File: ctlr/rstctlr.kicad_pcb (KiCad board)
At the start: 2 copper layers, 114.3 x 63.5 mm, 95 parts, among them J1 USB_B, J3 ICSP, U1 FT232RL, U10 LTV-827S, U11 LTV-827S, U12 LTV-827S, U2 MIC2025-1YM, U3 ATtiny2313A-20SU, U4 TLC59281, U5 LTV-827S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

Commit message: Update to KiCad6.
Signed-off-by: Dan Cross <cross@gajendra.net>
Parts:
- moved C4 7.93 mm to (78.2, 72.7)
- moved C5 7.93 mm to (86.8, 83.7)
- moved J3 7.93 mm to (97.0, 88.8)
- moved R7 7.93 mm to (93.5, 72.7)
- moved R8 7.93 mm to (101.7, 77.6)
- moved U1 7.93 mm to (80.3, 80.4)
- moved C2 7.93 mm to (75.8, 71.9)
- moved C3 7.93 mm to (80.5, 71.9)
- moved FB1 7.93 mm to (78.2, 71.9)
- moved R6 7.93 mm to (83.9, 71.9)
- moved C6 7.93 mm to (93.5, 77.0)
- moved C7 7.93 mm to (98.6, 69.9)
- moved D4 7.93 mm to (79.8, 88.6)
- moved D5 7.93 mm to (84.3, 88.6)
- moved J2 7.93 mm to (87.5, 67.9)
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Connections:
- U1 pad 10: Net-(U1-Pad10) -> unconnected-(U1-Pad10)
- U1 pad 11: Net-(U1-Pad11) -> unconnected-(U1-Pad11)
- U1 pad 13: Net-(U1-Pad13) -> unconnected-(U1-Pad13)
- U1 pad 2: Net-(U1-Pad2) -> unconnected-(U1-Pad2)
- U1 pad 24: Net-(U1-Pad24) -> unconnected-(U1-Pad24)
- U1 pad 27: Net-(U1-Pad27) -> unconnected-(U1-Pad27)
- U1 pad 28: Net-(U1-Pad28) -> unconnected-(U1-Pad28)
- U1 pad 3: Net-(U1-Pad3) -> unconnected-(U1-Pad3)
- U1 pad 6: Net-(U1-Pad6) -> unconnected-(U1-Pad6)
- U1 pad 8: Net-(U1-Pad8) -> unconnected-(U1-Pad8)
- U1 pad 9: Net-(U1-Pad9) -> unconnected-(U1-Pad9)
- U2 pad 2: Net-(U2-Pad2) -> unconnected-(U2-Pad2)
- U2 pad 4: Net-(U2-Pad4) -> unconnected-(U2-Pad4)
- U2 pad 5: Net-(U2-Pad5) -> unconnected-(U2-Pad5)
- U3 pad 11: Net-(U3-Pad11) -> unconnected-(U3-Pad11)
- U3 pad 16: Net-(U3-Pad16) -> unconnected-(U3-Pad16)
- U3 pad 4: Net-(U3-Pad4) -> unconnected-(U3-Pad4)
- U3 pad 6: Net-(U3-Pad6) -> unconnected-(U3-Pad6)
- U3 pad 7: Net-(U3-Pad7) -> unconnected-(U3-Pad7)
- U3 pad 8: Net-(U3-Pad8) -> unconnected-(U3-Pad8)
- U3 pad 9: Net-(U3-Pad9) -> unconnected-(U3-Pad9)
- U4 pad 22: Net-(U4-Pad22) -> unconnected-(U4-Pad22)
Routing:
- net Net-(C6-Pad1): track 289.3 -> 278.1 mm
- net Net-(D3-Pad1): track 13.8 -> 6.69 mm
- net Net-(C2-Pad1): track 15.0 -> 8.52 mm
- net Net-(D2-Pad1): track 16.1 -> 9.70 mm
- net Net-(U3-Pad13): track 38.8 -> 40.6 mm
- net Net-(J3-Pad5): track 25.6 -> 26.7 mm
- net Net-(R8-Pad1): track 37.3 -> 38.4 mm
- net Net-(U3-Pad12): track 35.1 -> 36.1 mm
- net Net-(D41-Pad1): track 10.8 -> 9.90 mm
- net Net-(D21-Pad2): track 5.61 -> 4.75 mm
- net Net-(D40-Pad1): track 9.78 -> 8.92 mm
- net Net-(D43-Pad1): track 10.9 -> 10.1 mm
- net Net-(D39-Pad1): track 10.9 -> 10.1 mm
- net Net-(D19-Pad1): track 13.0 -> 12.2 mm
- net Net-(D40-Pad2): track 9.71 -> 8.96 mm
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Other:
- net class Default removed

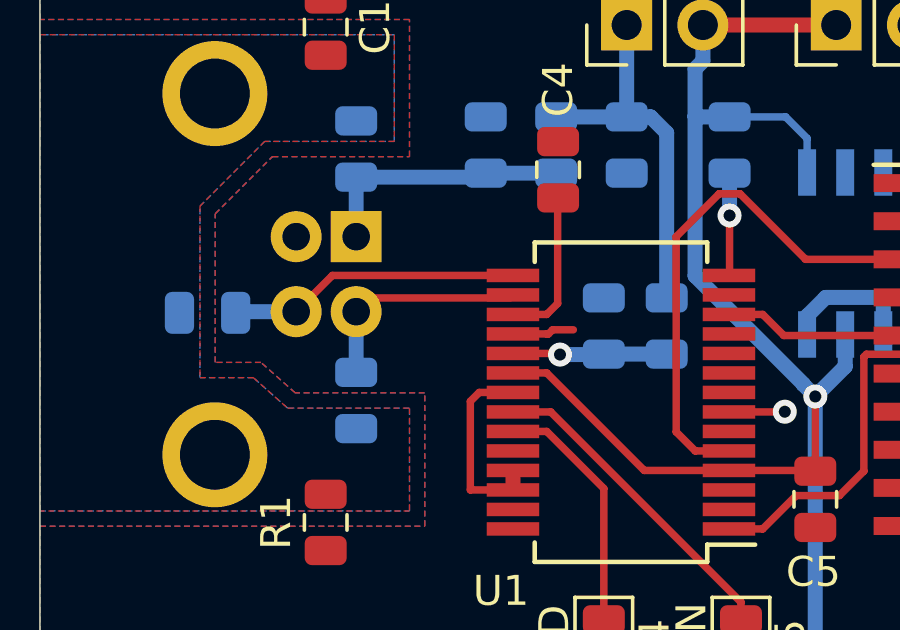
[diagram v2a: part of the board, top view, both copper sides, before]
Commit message: rstctlr: adjust USB trace length, fix stylesheets
Signed-off-by: Dan Cross <cross@gajendra.net>
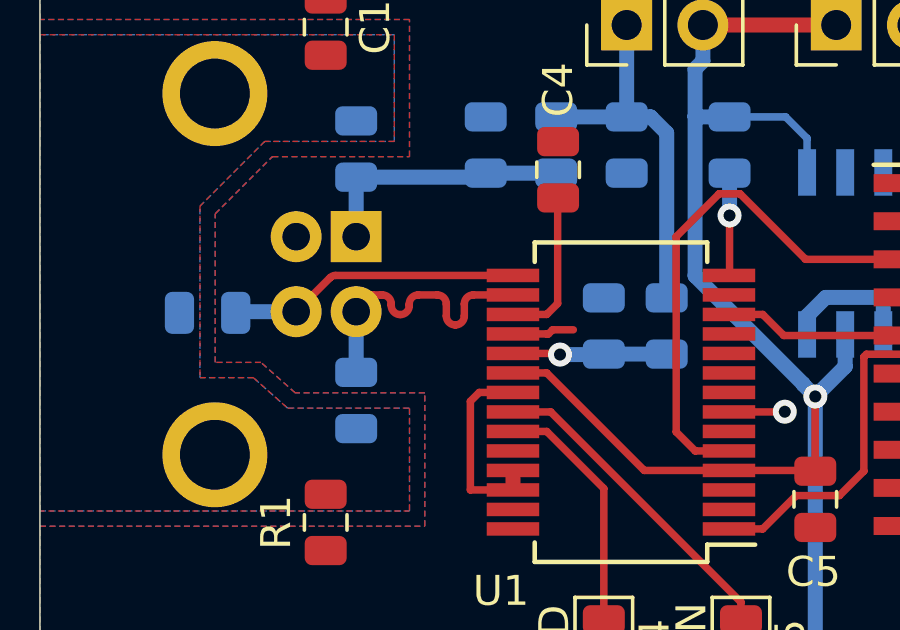
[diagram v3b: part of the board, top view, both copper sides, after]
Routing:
- net Net-(D3-Pad1): track 6.69 -> 9.66 mm
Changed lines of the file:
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@@
   (segment (start 92.5345 76.955) (end 89.027 76.955) (width 0.5) (layer "B.Cu") (net 6))
   (segment (start 86.53142 77.575137) (end 86.53142 78.665139) (width 0.5) (layer "B.Cu") (net 6))
-  (segment (start 70.7085 76.2225) (end 76.7275 76.2225) (width 0.25) (layer "F.Cu") (net 7))
-  (segment (start 69.501 77.43) (end 70.7085 76.2225) (width 0.25) (layer "F.Cu") (net 7))
+  (segment (start 70.635276 76.295724) (end 69.501 77.43) (width 0.25) (layer "F.Cu") (net 7))
+  (segment (start 76.7275 76.2225) (end 70.812053 76.2225) (width 0.25) (layer "F.Cu") (net 7))
+  (arc (start 70.635276 76.295724) (mid 70.716382 76.241531) (end 70.812053 76.2225) (width 0.25) (layer "F.Cu") (net 7))
   (segment (start 69.501 77.43) (end 67.5255 77.43) (width 0.5) (layer "B.Cu") (net 7))
-  (segment (start 71.958011 76.972989) (end 76.627011 76.972989) (width 0.25) (layer "F.Cu") (net 8))
+  (segment (start 72.3205 76.8725) (end 72.0585 76.8725) (width 0.25) (layer "F.Cu") (net 8))
+  (segment (start 72.0585 76.8725) (end 71.501 77.43) (width 0.25) (layer "F.Cu") (net 8))
+  (segment (start 72.6705 77.227314) (end 72.6705 77.1725) (width 0.25) (layer "F.Cu") (net 8))
+  (segment (start 74.5055 77.5725) (end 74.5055 77.1725) (width 0.25) (layer "F.Cu") (net 8))
+  (segment (start 74.2055 76.8725) (end 73.5705 76.8725) (width 0.25) (layer "F.Cu") (net 8))
+  (segment (start 72.3705 76.8725) (end 72.3205 76.8725) (width 0.25) (layer "F.Cu") (net 8))
+  (segment (start 73.2705 77.1725) (end 73.2705 77.227314) (width 0.25) (layer "F.Cu") (net 8))
+  (segment (start 76.7275 76.8725) (end 75.4055 76.8725) (width 0.25) (layer "F.Cu") (net 8))
+  (segment (start 75.1055 77.1725) (end 75.1055 77.5725) (width 0.25) (layer "F.Cu") (net 8))
+  (arc (start 75.1055 77.5725) (mid 75.017632 77.784632) (end 74.8055 77.8725) (width 0.25) (layer "F.Cu") (net 8))
+  (arc (start 72.6705 77.1725) (mid 72.582632 76.960368) (end 72.3705 76.8725) (width 0.25) (layer "F.Cu") (net 8))
+  (arc (start 73.2705 77.227314) (mid 73.182632 77.439446) (end 72.9705 77.527314) (width 0.25) (layer "F.Cu") (net 8))
+  (arc (start 74.5055 77.1725) (mid 74.417632 76.960368) (end 74.2055 76.8725) (width 0.25) (layer "F.Cu") (net 8))
+  (arc (start 73.5705 76.8725) (mid 73.358368 76.960368) (end 73.2705 77.1725) (width 0.25) (layer "F.Cu") (net 8))
+  (arc (start 75.4055 76.8725) (mid 75.193368 76.960368) (end 75.1055 77.1725) (width 0.25) (layer "F.Cu") (net 8))
+  (arc (start 74.8055 77.8725) (mid 74.593368 77.784632) (end 74.5055 77.5725) (width 0.25) (layer "F.Cu") (net 8))
+  (arc (start 72.9705 77.527314) (mid 72.758368 77.439446) (end 72.6705 77.227314) (width 0.25) (layer "F.Cu") (net 8))
   (segment (start 71.501 79.4535) (end 71.501 77.43) (width 0.5) (layer "B.Cu") (net 8))
   (segment (start 79.756 91.5115) (end 79.756 89.5765) (width 0.25) (layer "F.Cu") (net 9))
@@
   (segment (start 79.756 78.845) (end 81.8515 78.845) (width 0.5) (layer "B.Cu") (net 81))
   (segment (start 78.2955 78.86) (end 79.741 78.86) (width 0.5) (layer "B.Cu") (net 81))
-  (segment (start 79.741 78.86) (end 79.756 78.845) (width 0.25) (layer "B.Cu") (net 81))
   (segment (start 83.947 74.2245) (end 83.947 76.203) (width 0.25) (layer "F.Cu") (net 82))
   (via (at 83.947 74.2245) (size 0.8) (drill 0.4) (layers "F.Cu" "B.Cu") (net 82))

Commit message: rstctlr: bump version number.
Signed-off-by: Dan Cross <cross@gajendra.net>
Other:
- board text added: "RST/PWR Controller V3.0"
- board text removed: "RST/PWR Controller V2.0"
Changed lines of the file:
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@@
   (gr_line (start 175.26 107.95) (end 60.96 107.95) (layer "Edge.Cuts") (width 0.05))
   (gr_line (start 60.96 107.95) (end 60.96 44.45) (layer "Edge.Cuts") (width 0.05))
-  (gr_text "RST/PWR Controller\nV2.0" (at 84.6836 51.1556) (layer "F.SilkS")
+  (gr_text "RST/PWR Controller\nV3.0" (at 84.6836 51.1556) (layer "F.SilkS")
     (effects (font (size 1.5 1.5) (thickness 0.3)))
   )
